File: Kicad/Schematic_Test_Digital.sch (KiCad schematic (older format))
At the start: 74 parts, among them J301 I2C_CONNECTOR_OUT, J302 I2C_CONNECTOR_OUT, J303 SWD_DEBUG, J304 CONN_JOYSTICK, J305 I2C_CONNECTOR_OUT, SW301 RESET PUSH, U301 TSX-3225, U302 LIS3MDLTR, U303 LSM6DS33TR, U304 74HC595PW, U305 74HC595PW, U306 74HC595PW

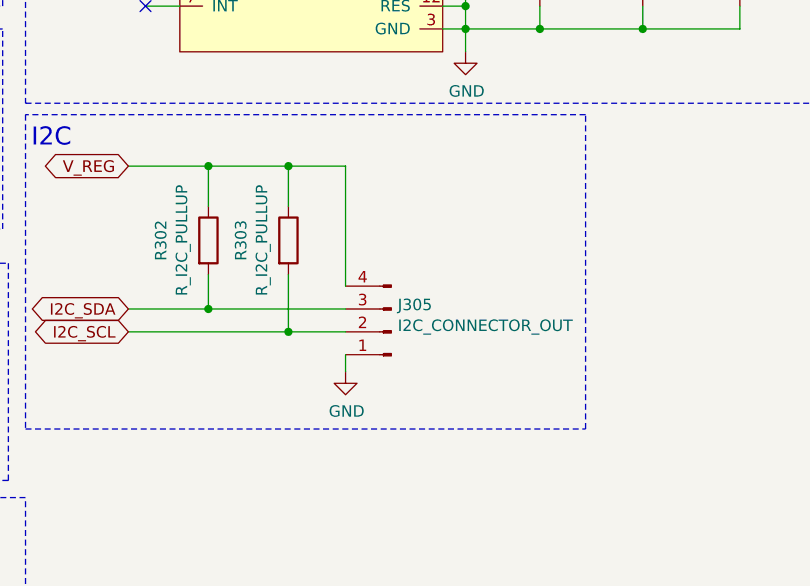
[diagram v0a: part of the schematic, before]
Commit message: Many parts are now placed on PCB.
Work left off on MC, gyro, and mag.

Discovered free-angle mode for traces, which will make connections look better in the future.
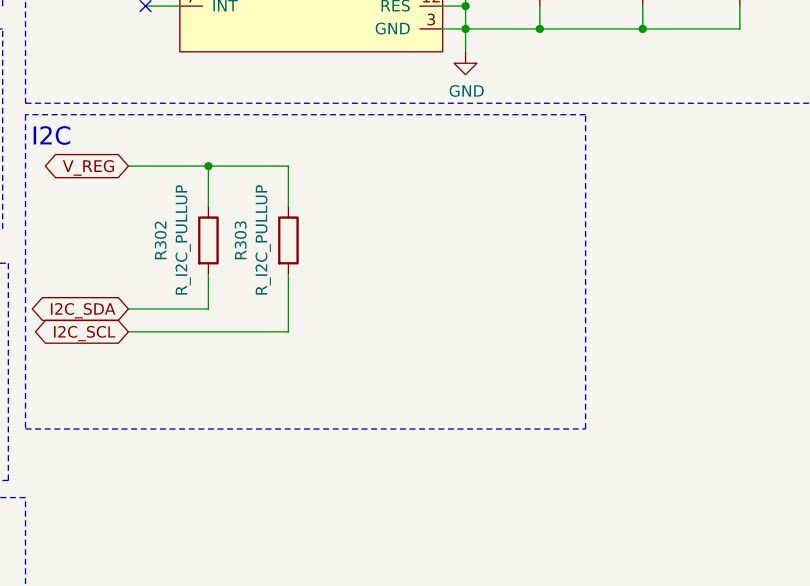
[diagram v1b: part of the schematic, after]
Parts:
- removed J305: I2C_CONNECTOR_OUT, Connector_JST:JST_EH_B4B-EH-A_1x04_P2.50mm_Vertical, symbol Connector:Conn_01x04_Male
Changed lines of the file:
@@
 Wire Notes Line
 	2350 4975 2350 6350
-$Comp
-L power:GND #PWR?
-U 1 1 5F64B49D
-P 3750 6100
-AR Path="/5F64B49D" Ref="#PWR?"  Part="1"
-AR Path="/5F580392/5F64B49D" Ref="#PWR0310"  Part="1"
-F 0 "#PWR0310" H 3750 5850 50  0001 C CNN
-F 1 "GND" H 3755 5927 50  0000 C CNN
-F 2 "" H 3750 6100 50  0001 C CNN
-F 3 "" H 3750 6100 50  0001 C CNN
-	1    3750 6100
-	1    0    0    -1
-$EndComp
-Wire Wire Line
-	3750 6025 3750 6100
-Wire Wire Line
-	3750 5200 3750 5725
-Wire Wire Line
-	3150 5825 3750 5825
-Wire Wire Line
-	3500 5925 3750 5925
-Connection ~ 3500 5925
-Connection ~ 3150 5825
-$Comp
-L Connector:Conn_01x04_Male J?
-U 1 1 5F64B4A9
-P 3950 5925
-AR Path="/5F64B4A9" Ref="J?"  Part="1"
-AR Path="/5F580392/5F64B4A9" Ref="J305"  Part="1"
-F 0 "J305" H 3922 5807 50  0000 R CNN
-F 1 "I2C_CONNECTOR_OUT" H 3922 5898 50  0000 R CNN
-F 2 "Connector_JST:JST_EH_B4B-EH-A_1x04_P2.50mm_Vertical" H 3950 5925 50  0001 C CNN
-F 3 "~" H 3950 5925 50  0001 C CNN
-F 4 "JST - 4 pin" H 3950 5925 50  0001 C CNN "part_details"
-F 5 "LOCAL STOCK" H 3950 5925 50  0001 C CNN "part_url"
-	1    3950 5925
-	-1   0    0    1
-$EndComp
-Connection ~ 3500 5200
-Wire Wire Line
-	3500 5200 3750 5200
 Wire Wire Line
 	3500 5675 3500 5925

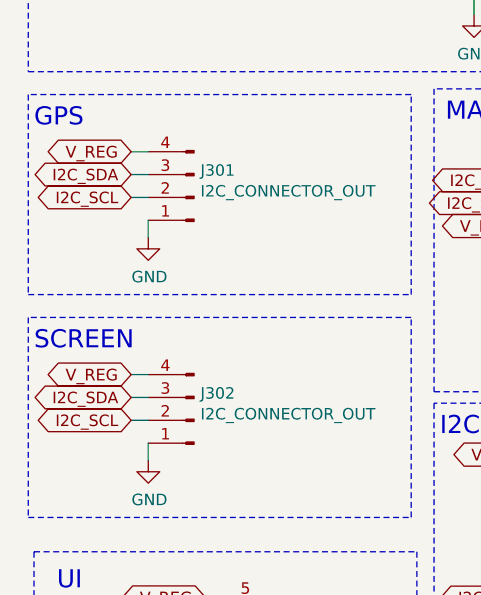
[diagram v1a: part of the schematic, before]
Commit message: All parts on board and routed.  Beginning final part compatibility check.  Big TODO is select GPS, verify parts, and begin route-polish step.
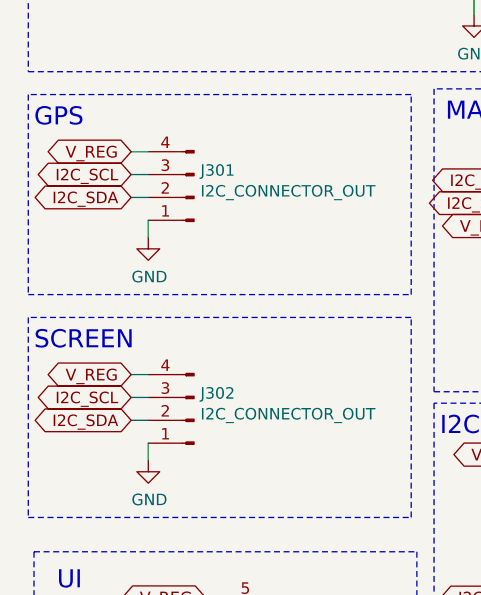
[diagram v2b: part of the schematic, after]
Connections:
- net I2C_SCL: now also J301.3 (Pin_3), J302.3 (Pin_3); no longer J301.2 (Pin_2), J302.2 (Pin_2)
- net I2C_SDA: now also J301.2 (Pin_2), J302.2 (Pin_2); no longer J301.3 (Pin_3), J302.3 (Pin_3)
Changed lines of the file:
@@
 Text Notes 600  4750 0    79   ~ 0
 SCREEN\n
+Text GLabel 1025 5050 0    50   BiDi ~ 0
+I2C_SDA
 Text GLabel 1025 4950 0    50   BiDi ~ 0
-I2C_SDA
-Text GLabel 1025 5050 0    50   BiDi ~ 0
 I2C_SCL
 Text GLabel 1025 4850 0    51   BiDi ~ 0
@@
 Text Notes 600  3775 0    79   ~ 0
 GPS\n
+Text GLabel 1025 4075 0    50   BiDi ~ 0
+I2C_SDA
 Text GLabel 1025 3975 0    50   BiDi ~ 0
-I2C_SDA
-Text GLabel 1025 4075 0    50   BiDi ~ 0
 I2C_SCL
 Text GLabel 1025 3875 0    51   BiDi ~ 0

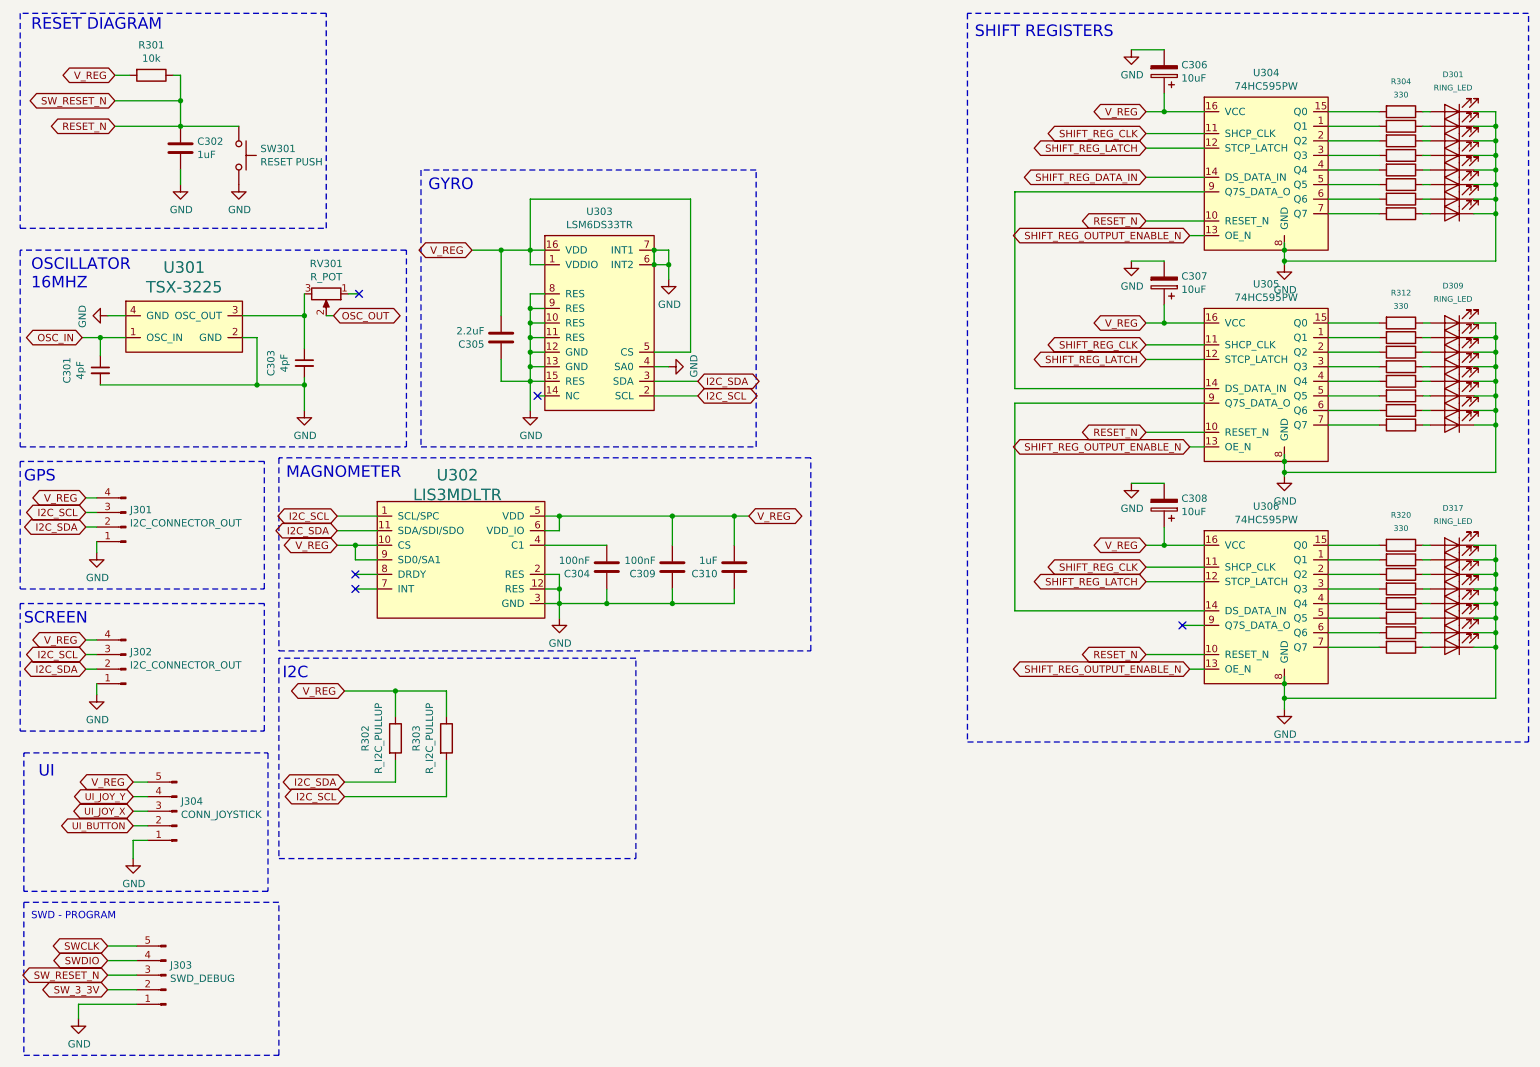
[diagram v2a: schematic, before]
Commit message: Calculating ram needed and current selected chip will not fit it.  Upgrading to a more capable chip.
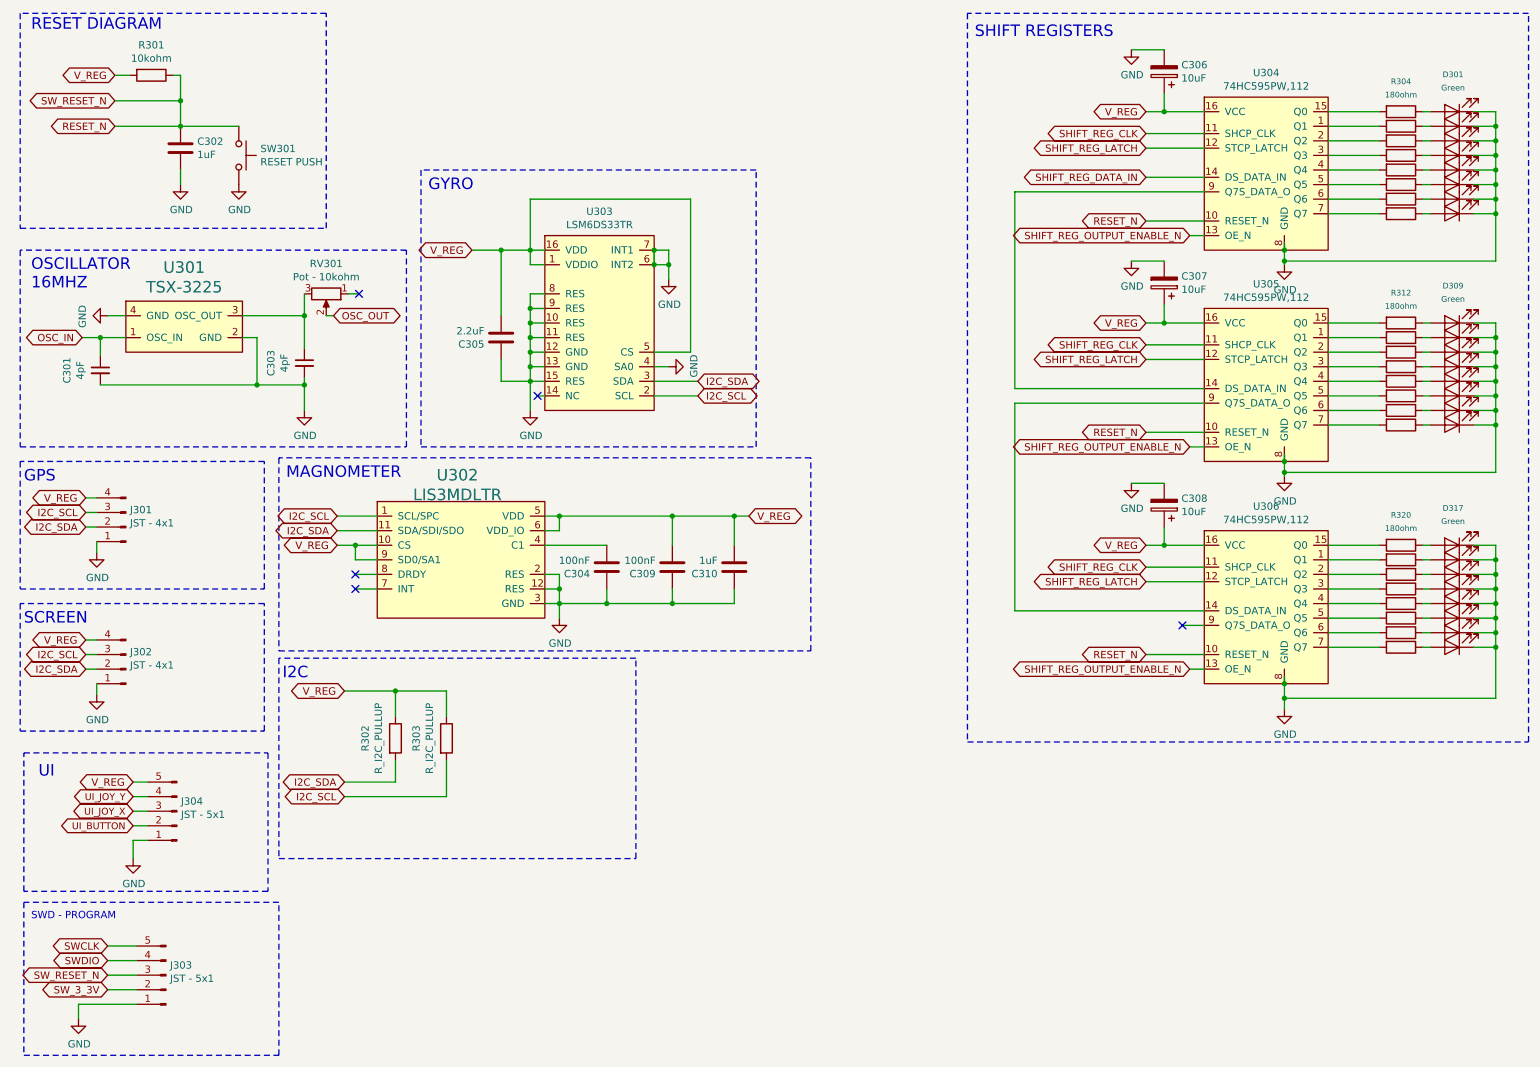
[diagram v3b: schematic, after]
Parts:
- C310: part_url https://www.digikey.com/product-detail/en/w%C3%BCrth-elektronik/885012107001/732-7612-1-ND/5454239 -> https://www.digikey.com/product-detail/en/w%C3%BCrth-elektronik/885012107015/732-7625-1-ND/5454252
- D301, D302, D303, D304, D305, D306, D307, D308, D309, D310, D311, D312, D313, D314, D315, D316, D317, D318, D319, D320, D321, D322, D323, D324: value RING_LED -> Green; part_name LED - Green -> LED - Ring Green
- J301: value I2C_CONNECTOR_OUT -> JST - 4x1; part_details JST - 4 pin -> (none); part_name (none) -> GPS Connector; part_url LOCAL STOCK -> (none)
- J302: value I2C_CONNECTOR_OUT -> JST - 4x1; part_details JST - 4 pin -> (none); part_name (none) -> Screen Connector; part_url LOCAL STOCK -> (none)
- J303: value SWD_DEBUG -> JST - 5x1; part_name (none) -> SWD Program Connector; part_url LOCAL STOCK -> (none)
- J304: value CONN_JOYSTICK -> JST - 5x1; part_details JST - 5 pin -> (none); part_name (none) -> Joystick Connector; part_url LOCAL STOCK -> (none)
- R301: value 10k -> 10kohm
- R304, R305, R306, R307, R308, R309, R310, R311, R312, R313, R314, R315, R316, R317, R318, R319, R320, R321, R322, R323, R324, R325, R326, R327: value 330 -> 180ohm; part_details Limits current to 8mA -> LED dropout: 2v. V_REG is 2.8v. 0.8/180 = 4.4mA; part_url https://www.digikey.com/product-detail/en/yageo/RC1206FR-07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 -> https://www.digikey.com/product-detail/en/stackpole-electro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
- RV301: value R_POT -> Pot - 10kohm
- SW301: part_name Push Switch -> Switch - Reset (internal)
- U301: part_details 16MHz Crystal -> (none); part_name TSX-3225 -> 16MHz Crystal
- U302: part_details Magnometer Sensor -> (none); part_name LIS3MDLTR -> Magnometer Sensor
- U303: part_details 6-axis Gyrometer -> (none); part_name LSM6DS33TR -> 6-axis Gyrometer
- U304, U305, U306: value 74HC595PW -> 74HC595PW,112; part_details Shift Register -> (none); part_name 74HC595PW,118 -> Shift Register

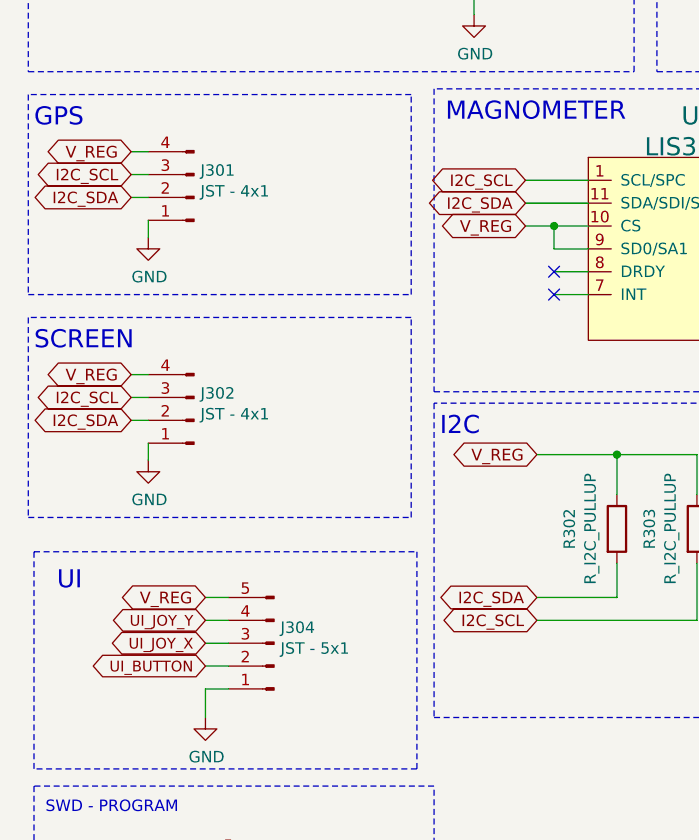
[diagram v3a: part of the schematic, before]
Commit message: Upgraded to STM32G0 for increased memory. Schematic and PCB are updated.  PCB now has radial grid applied in preparation of final part placement.
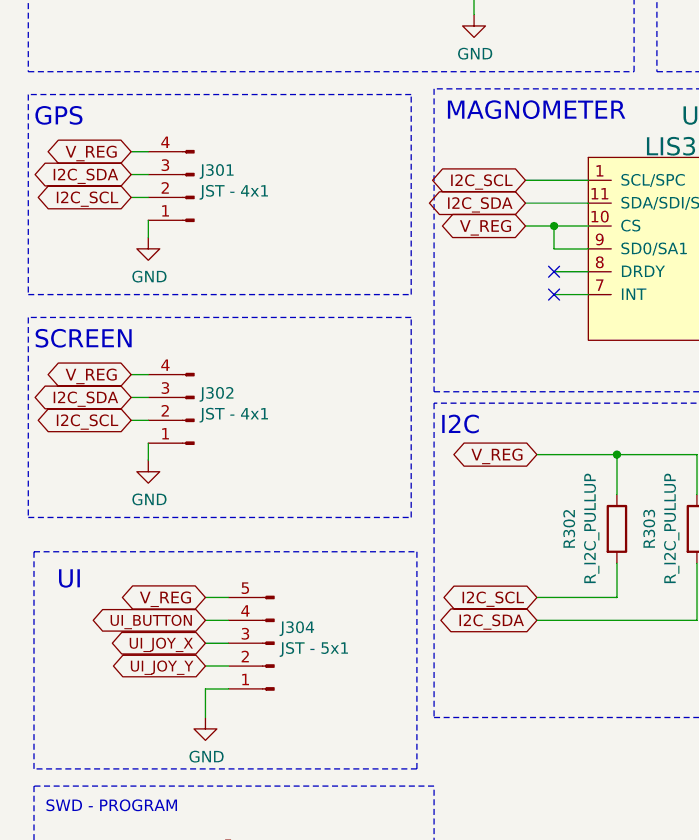
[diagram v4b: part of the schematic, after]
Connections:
- net I2C_SCL: now also J301.2 (Pin_2), J302.2 (Pin_2), R302.2; no longer J301.3 (Pin_3), J302.3 (Pin_3), R303.2
- net I2C_SDA: now also J301.3 (Pin_3), J302.3 (Pin_3), R303.2; no longer J301.2 (Pin_2), J302.2 (Pin_2), R302.2
- net UI_BUTTON: now also J304.4 (Pin_4); no longer J304.2 (Pin_2)
- net UI_JOY_Y: now also J304.2 (Pin_2); no longer J304.4 (Pin_4)
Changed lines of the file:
@@
 	1    0    0    -1
 $EndComp
-Text GLabel 1350 5925 0    47   BiDi ~ 0
+Text GLabel 1350 6125 0    47   BiDi ~ 0
 UI_JOY_Y
 Text GLabel 1350 6025 0    47   BiDi ~ 0
 UI_JOY_X
-Text GLabel 1350 6125 0    47   BiDi ~ 0
+Text GLabel 1350 5925 0    47   BiDi ~ 0
 UI_BUTTON
 Text Notes 7125 725  0    79   ~ 0
@@
 Text Notes 600  4750 0    79   ~ 0
 SCREEN\n
+Text GLabel 1025 4950 0    50   BiDi ~ 0
+I2C_SDA
 Text GLabel 1025 5050 0    50   BiDi ~ 0
-I2C_SDA
-Text GLabel 1025 4950 0    50   BiDi ~ 0
 I2C_SCL
 Text GLabel 1025 4850 0    51   BiDi ~ 0
@@
 Text Notes 600  3775 0    79   ~ 0
 GPS\n
+Text GLabel 1025 3975 0    50   BiDi ~ 0
+I2C_SDA
 Text GLabel 1025 4075 0    50   BiDi ~ 0
-I2C_SDA
-Text GLabel 1025 3975 0    50   BiDi ~ 0
 I2C_SCL
 Text GLabel 1025 3875 0    51   BiDi ~ 0
@@
 Wire Wire Line
 	2800 5825 3150 5825
+Text GLabel 2800 5925 0    50   BiDi ~ 0
+I2C_SDA
 Text GLabel 2800 5825 0    50   BiDi ~ 0
-I2C_SDA
-Text GLabel 2800 5925 0    50   BiDi ~ 0
 I2C_SCL
 Text GLabel 2800 5200 0    51   BiDi ~ 0

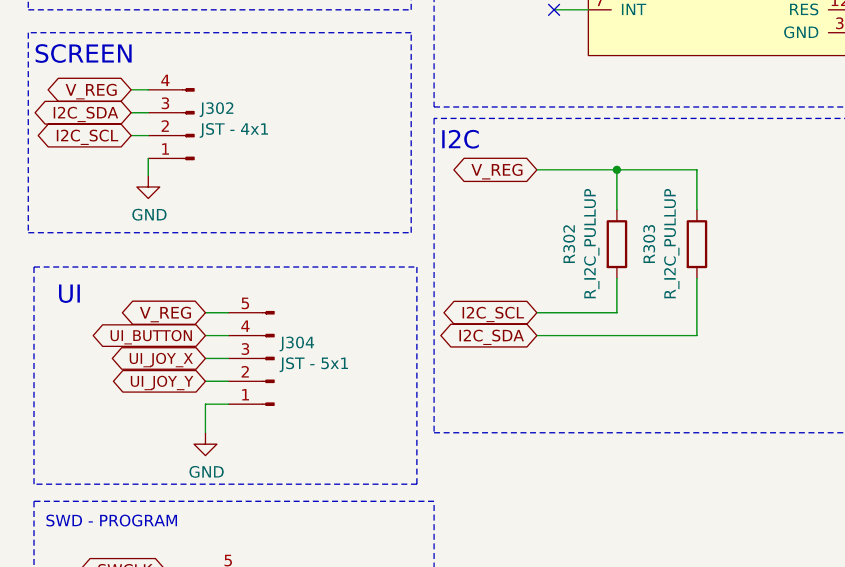
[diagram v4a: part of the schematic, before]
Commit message: Continued work on PCB.  Added back art.
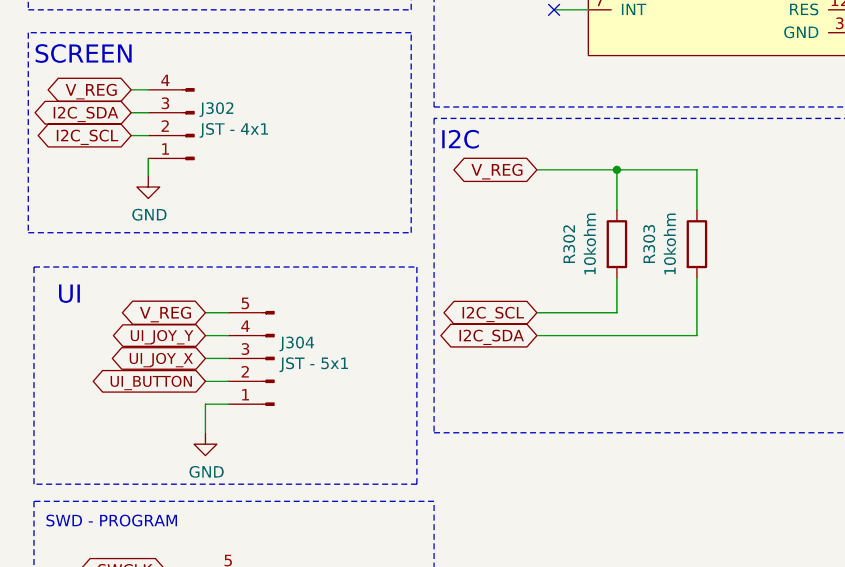
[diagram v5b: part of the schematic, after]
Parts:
- J302: part_url (none) -> https://www.amazon.com/WayinTop-Display-SSD1306-3-3V-5V-Ras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
- R302, R303: value R_I2C_PULLUP -> 10kohm; part_name (none) -> Resistor - Pull up; part_url (none) -> https://www.digikey.com/product-detail/en/yageo/RC1206JR-07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
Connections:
- net UI_BUTTON: now also J304.2 (Pin_2); no longer J304.4 (Pin_4)
- net UI_JOY_Y: now also J304.4 (Pin_4); no longer J304.2 (Pin_2)
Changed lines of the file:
@@
 	1    0    0    -1
 $EndComp
-Text GLabel 1350 6125 0    47   BiDi ~ 0
+Text GLabel 1350 5925 0    47   BiDi ~ 0
 UI_JOY_Y
 Text GLabel 1350 6025 0    47   BiDi ~ 0
 UI_JOY_X
-Text GLabel 1350 5925 0    47   BiDi ~ 0
+Text GLabel 1350 6125 0    47   BiDi ~ 0
 UI_BUTTON
 Text Notes 7125 725  0    79   ~ 0
@@
 F 3 "~" H 1300 5050 50  0001 C CNN
 F 4 "" H 1300 5050 50  0001 C CNN "part_details"
-F 5 "" H 1300 5050 50  0001 C CNN "part_url"
+F 5 "https://www.amazon.com/WayinTop-Display-SSD1306-3-3V-5V-Raspberry/dp/B085NHJYBV/ref=pd_vtp_328_10?_encoding=UTF8&pd_rd_i=B085NHM5TC&pd_rd_r=7bdf7370-03dc-4b29-82c0-f607778b8952&pd_rd_w=HTH0F&pd_rd_wg=QAfMe&pf_rd_p=9f0d957d-c466-420a-817f-4adcb2657c85&pf_rd_r=2740EXSJPY7P7H0NYG2V&refRID=2740EXSJPY7P7H0NYG2V&th=1" H 1300 5050 50  0001 C CNN "part_url"
 F 6 "Screen Connector" H 1300 5050 50  0001 C CNN "part_name"
 	1    1300 5050
@@
 AR Path="/5F580392/5F64B4C2" Ref="R303"  Part="1"
 F 0 "R303" V 3293 5525 50  0000 C CNN
-F 1 "R_I2C_PULLUP" V 3384 5525 50  0000 C CNN
+F 1 "10kohm" V 3384 5525 50  0000 C CNN
 F 2 "Resistor_SMD:R_1206_3216Metric_Pad1.42x1.75mm_HandSolder" V 3430 5525 50  0001 C CNN
 F 3 "~" H 3500 5525 50  0001 C CNN
+F 4 "Resistor - Pull up" H 3500 5525 50  0001 C CNN "part_name"
+F 5 "https://www.digikey.com/product-detail/en/yageo/RC1206JR-0710KL/311-10KERCT-ND/732156" H 3500 5525 50  0001 C CNN "part_url"
 	1    3500 5525
 	1    0    0    -1
@@
 AR Path="/5F580392/5F64B4C8" Ref="R302"  Part="1"
 F 0 "R302" V 2943 5525 50  0000 C CNN
-F 1 "R_I2C_PULLUP" V 3034 5525 50  0000 C CNN
+F 1 "10kohm" V 3034 5525 50  0000 C CNN
 F 2 "Resistor_SMD:R_1206_3216Metric_Pad1.42x1.75mm_HandSolder" V 3080 5525 50  0001 C CNN
 F 3 "~" H 3150 5525 50  0001 C CNN
+F 4 "Resistor - Pull up" H 3150 5525 50  0001 C CNN "part_name"
+F 5 "https://www.digikey.com/product-detail/en/yageo/RC1206JR-0710KL/311-10KERCT-ND/732156" H 3150 5525 50  0001 C CNN "part_url"
 	1    3150 5525
 	1    0    0    -1
